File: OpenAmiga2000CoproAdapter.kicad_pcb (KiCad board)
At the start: 2 copper layers, 188.6 x 110.4 mm, 75 parts, among them CN1 A2000_COPRO_SLOT, P1 CONN_2, P10 CONN_1, P11 CONN_1, P12 CONN_1, P13 CONN_1, P14 CONN_1, P15 CONN_1, P2 CONN_2, P3 CONN_2, P4 CONN_2, P5 CONN_1, P6 CONN_1, P7 CONN_1, P8 CONN_1, P9 CONN_1, P99 OSHW_LOGO, U1 68000D, U10 Spare, U11 74HCT00, U12 74HCT27, U13 74HCT74, U14 74F86, U15 74F74, U16 74HCT04, U17 74HCT112, U18 74F157, U19 74F157, U2 AS6C4008-55PCN, U3 AS6C4008-55PCN, U4 AS6C4008-55PCN, U5 AS6C4008-55PCN, U6 74HCT00, U7 74HCT32, U8 74HCT32, U9 74LS05

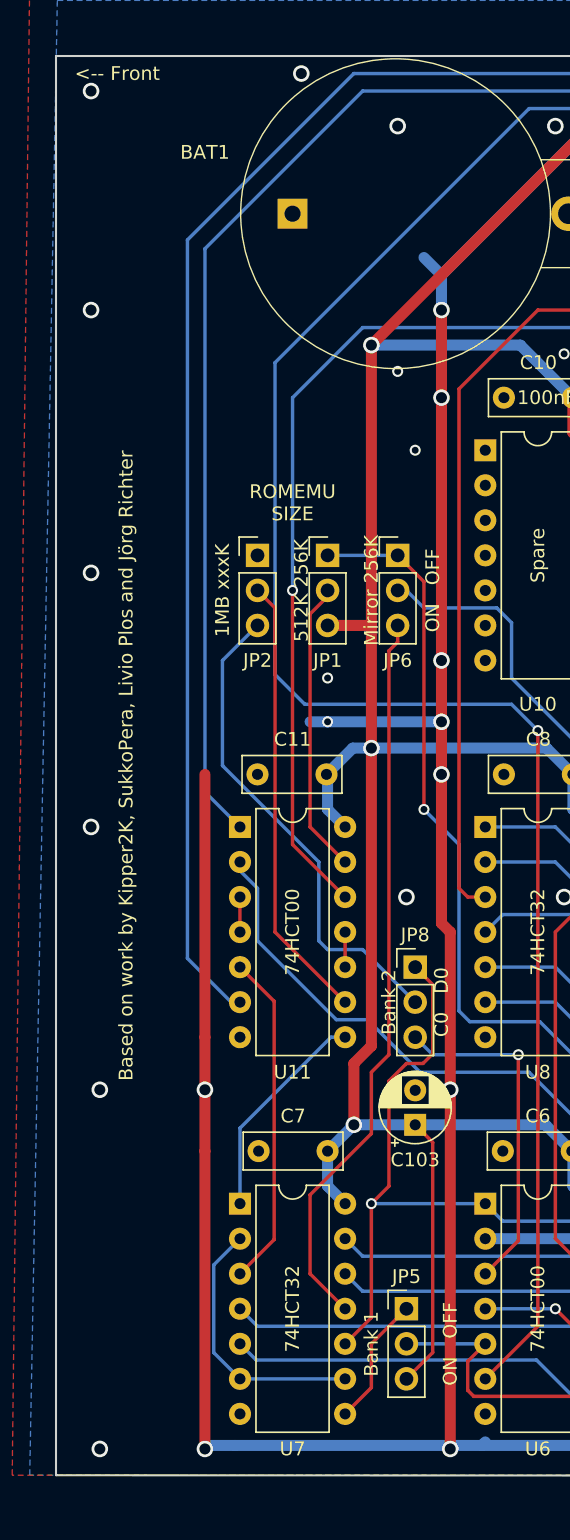
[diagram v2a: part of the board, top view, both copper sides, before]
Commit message: more via fixing
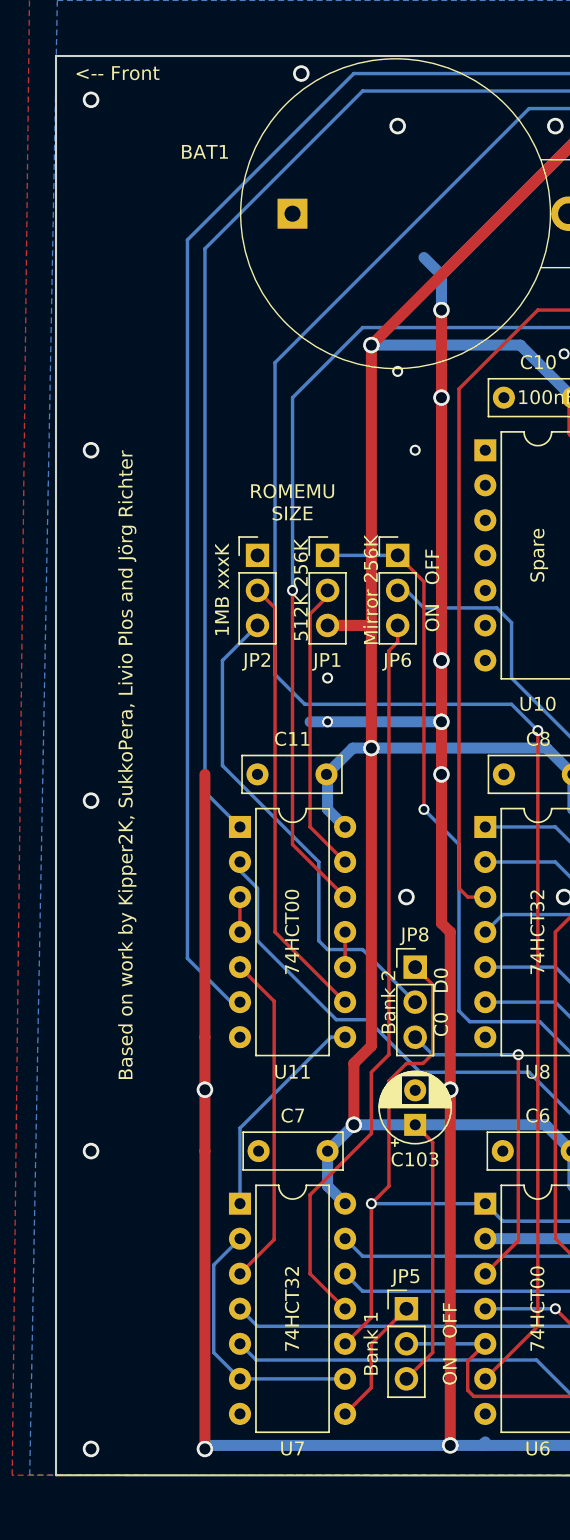
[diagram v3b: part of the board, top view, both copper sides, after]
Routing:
- net GND: track 1168.9 -> 1168.5 mm, vias 158 -> 157
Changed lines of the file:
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@@
   (segment (start 108.458 138.1125) (end 107.2515 136.906) (width 0.8) (layer B.Cu) (net 1))
   (segment (start 93.0275 136.906) (end 90.106496 136.906) (width 0.8) (layer B.Cu) (net 1))
-  (segment (start 90.106504 136.905992) (end 90.106496 136.906) (width 0.8) (layer B.Cu) (net 1))
-  (segment (start 90.106504 136.906) (end 90.106504 136.905992) (width 0.8) (layer B.Cu) (net 1))
   (segment (start 72.3265 136.652) (end 72.0725 136.906) (width 0.8) (layer B.Cu) (net 1))
-  (segment (start 72.0725 136.906) (end 90.106504 136.906) (width 0.8) (layer B.Cu) (net 1))
-  (segment (start 72.0725 136.906) (end 69.4055 136.906) (width 0.8) (layer B.Cu) (net 1))
   (segment (start 52.0065 107.315) (end 52.0065 115.57) (width 0.8) (layer F.Cu) (net 1))
   (segment (start 52.0065 115.57) (end 52.0065 136.906) (width 0.8) (layer F.Cu) (net 1))
-  (segment (start 54.1655 136.906) (end 52.0065 136.906) (width 0.8) (layer B.Cu) (net 1))
   (via (at 52.0065 137.16) (size 1.2) (drill 0.8) (layers F.Cu B.Cu) (net 1))
-  (via (at 69.7865 137.16) (size 1.2) (drill 0.8) (layers F.Cu B.Cu) (net 1))
-  (segment (start 54.1655 136.906) (end 69.7865 136.906) (width 0.8) (layer B.Cu) (net 1))
-  (segment (start 69.7865 136.906) (end 69.786502 136.906002) (width 0.8) (layer B.Cu) (net 1))
   (segment (start 52.0065 107.315) (end 52.0065 88.265) (width 0.8) (layer F.Cu) (net 1))
   (via (at 66.6115 97.155) (size 1.2) (drill 0.8) (layers F.Cu B.Cu) (net 1))
@@
   (via (at 69.7865 111.125) (size 1.2) (drill 0.8) (layers F.Cu B.Cu) (net 1))
   (segment (start 187.2615 103.505) (end 187.2615 103.505) (width 0.8) (layer F.Cu) (net 1))
-  (via (at 187.2615 103.505) (size 1.2) (drill 0.8) (layers F.Cu B.Cu) (net 1) (status 1000000))
+  (via (at 187.2615 103.505) (size 1.2) (drill 0.8) (layers F.Cu B.Cu) (net 1))
   (segment (start 189.8015 86.995) (end 189.8015 84.455) (width 0.8) (layer B.Cu) (net 1))
   (segment (start 187.2615 84.455) (end 189.8015 84.455) (width 0.8) (layer B.Cu) (net 1))
@@
   (segment (start 213.9315 45.72) (end 213.9315 45.72) (width 0.8) (layer B.Cu) (net 1))
   (via (at 213.9315 45.72) (size 1.2) (drill 0.8) (layers F.Cu B.Cu) (net 1))
-  (via (at 44.3865 137.16) (size 1.2) (drill 0.8) (layers F.Cu B.Cu) (net 1))
-  (via (at 44.3865 111.125) (size 1.2) (drill 0.8) (layers F.Cu B.Cu) (net 1))
-  (via (at 43.7515 92.075) (size 1.2) (drill 0.8) (layers F.Cu B.Cu) (net 1))
+  (via (at 43.7515 137.16) (size 1.2) (drill 0.8) (layers F.Cu B.Cu) (net 1))
+  (via (at 43.7515 115.57) (size 1.2) (drill 0.8) (layers F.Cu B.Cu) (net 1))
+  (via (at 43.7515 90.17) (size 1.2) (drill 0.8) (layers F.Cu B.Cu) (net 1))
   (via (at 208.8515 52.705) (size 1.2) (drill 0.8) (layers F.Cu B.Cu) (net 1))
   (via (at 205.0415 57.785) (size 1.2) (drill 0.8) (layers F.Cu B.Cu) (net 1))
@@
   (via (at 118.6815 109.22) (size 1.2) (drill 0.8) (layers F.Cu B.Cu) (net 1))
   (via (at 52.0065 111.125) (size 1.2) (drill 0.8) (layers F.Cu B.Cu) (net 1))
-  (via (at 43.7515 54.61) (size 1.2) (drill 0.8) (layers F.Cu B.Cu) (net 1))
+  (via (at 43.7515 64.77) (size 1.2) (drill 0.8) (layers F.Cu B.Cu) (net 1))
   (via (at 169.4815 137.795) (size 0.8) (drill 0.5) (layers F.Cu B.Cu) (net 1))
   (segment (start 168.8465 137.16) (end 168.724159 137.037659) (width 0.8) (layer F.Cu) (net 1))
@@
   (via (at 83.7565 57.15) (size 1.2) (drill 0.8) (layers F.Cu B.Cu) (net 1))
   (via (at 184.7215 64.77) (size 1.2) (drill 0.8) (layers F.Cu B.Cu) (net 1))
-  (via (at 43.7515 38.735) (size 1.2) (drill 0.8) (layers F.Cu B.Cu) (net 1))
+  (via (at 43.7515 39.37) (size 1.2) (drill 0.8) (layers F.Cu B.Cu) (net 1))
   (via (at 58.9915 37.465) (size 1.2) (drill 0.8) (layers F.Cu B.Cu) (net 1))
   (via (at 194.8815 48.26) (size 1.2) (drill 0.8) (layers F.Cu B.Cu) (net 1))
@@
   (segment (start 187.2615 122.555) (end 187.2615 127.635) (width 0.8) (layer B.Cu) (net 1))
   (via (at 187.2615 127.635) (size 1.2) (drill 0.8) (layers F.Cu B.Cu) (net 1))
-  (via (at 43.7515 73.66) (size 1.2) (drill 0.8) (layers F.Cu B.Cu) (net 1))
   (via (at 174.5615 82.55) (size 1.2) (drill 0.8) (layers F.Cu B.Cu) (net 1))
   (via (at 184.0865 43.815) (size 1.2) (drill 0.8) (layers F.Cu B.Cu) (net 1))
   (via (at 179.6415 113.665) (size 1.2) (drill 0.8) (layers F.Cu B.Cu) (net 1))
+  (segment (start 90.106504 136.905992) (end 90.106496 136.906) (width 0.8) (layer B.Cu) (net 1))
+  (segment (start 90.106504 136.906) (end 90.106504 136.905992) (width 0.8) (layer B.Cu) (net 1))
+  (segment (start 72.0725 136.906) (end 90.106504 136.906) (width 0.8) (layer B.Cu) (net 1))
+  (via (at 69.786502 136.905998) (size 1.2) (drill 0.8) (layers F.Cu B.Cu) (net 1))
+  (segment (start 72.0725 136.906) (end 69.786504 136.906) (width 0.8) (layer B.Cu) (net 1))
+  (segment (start 69.786504 136.906) (end 69.786502 136.905998) (width 0.8) (layer B.Cu) (net 1))
+  (segment (start 69.786498 136.905998) (end 69.786502 136.906002) (width 0.8) (layer B.Cu) (net 1))
+  (segment (start 52.006502 136.905998) (end 69.786498 136.905998) (width 0.8) (layer B.Cu) (net 1))
+  (segment (start 52.0065 136.906) (end 52.006502 136.905998) (width 0.8) (layer B.Cu) (net 1))
   (segment (start 126.238 108.6485) (end 126.3015 108.585) (width 0.8) (layer F.Cu) (net 2))
   (segment (start 126.238 112.0775) (end 126.238 108.6485) (width 0.8) (layer F.Cu) (net 2))

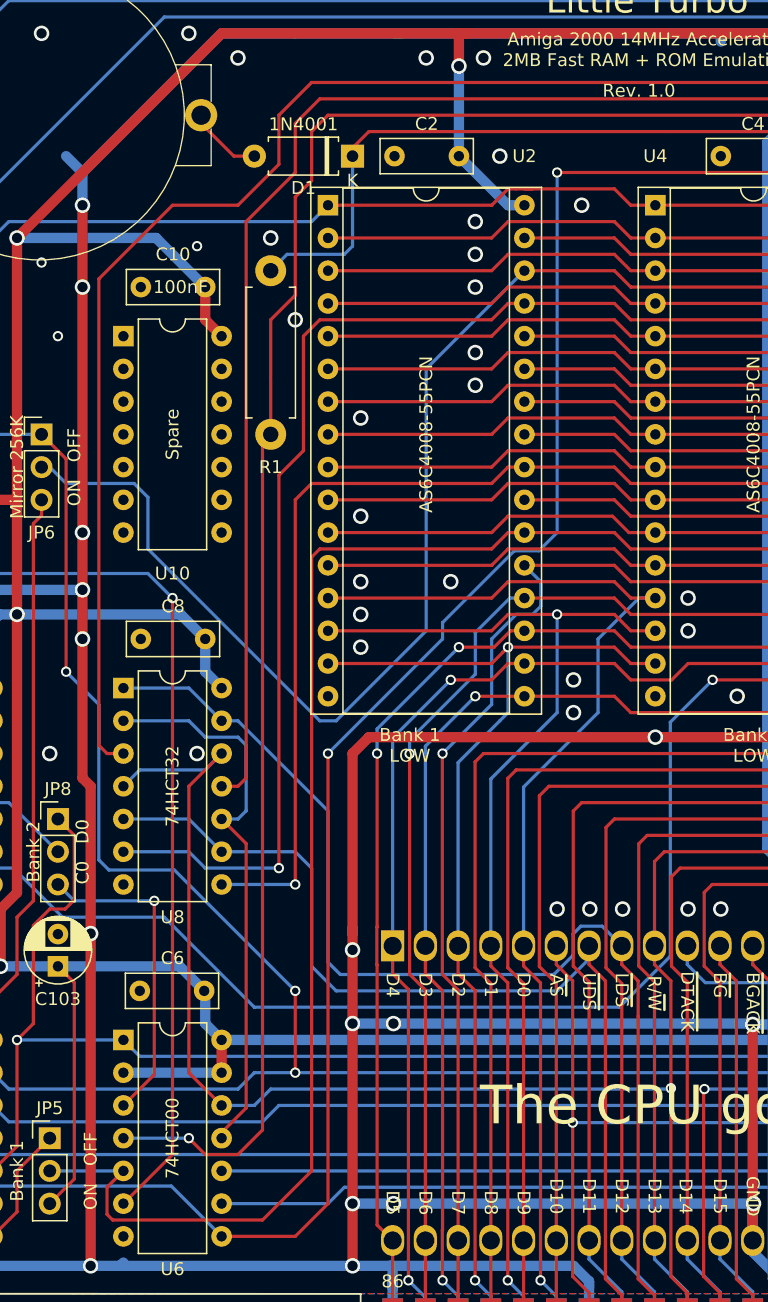
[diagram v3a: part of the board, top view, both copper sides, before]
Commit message: fix silkscreen label
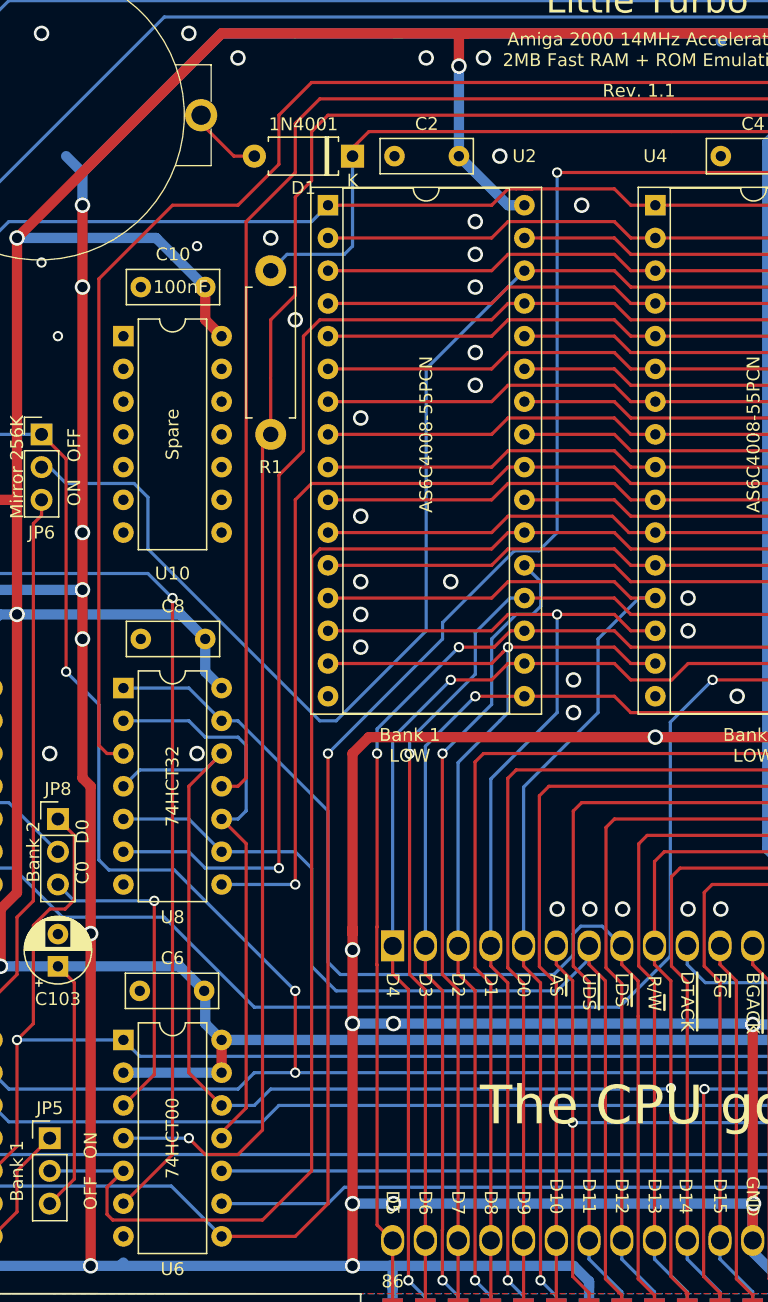
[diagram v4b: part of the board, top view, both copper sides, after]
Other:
- board text added: "OFF ON"
- board text added: "Rev. 1.1"
- board text removed: "Rev. 1.0"

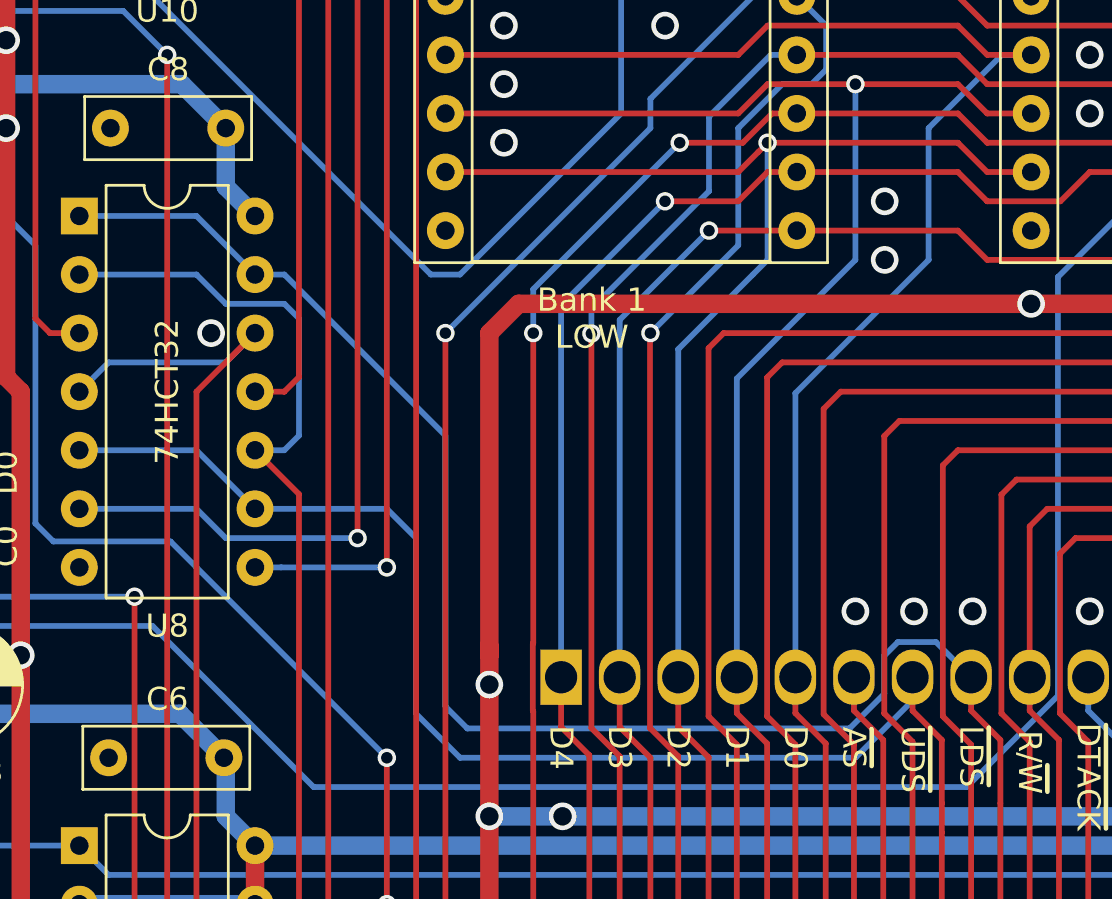
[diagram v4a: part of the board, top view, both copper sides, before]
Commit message: fix uds lds mixup
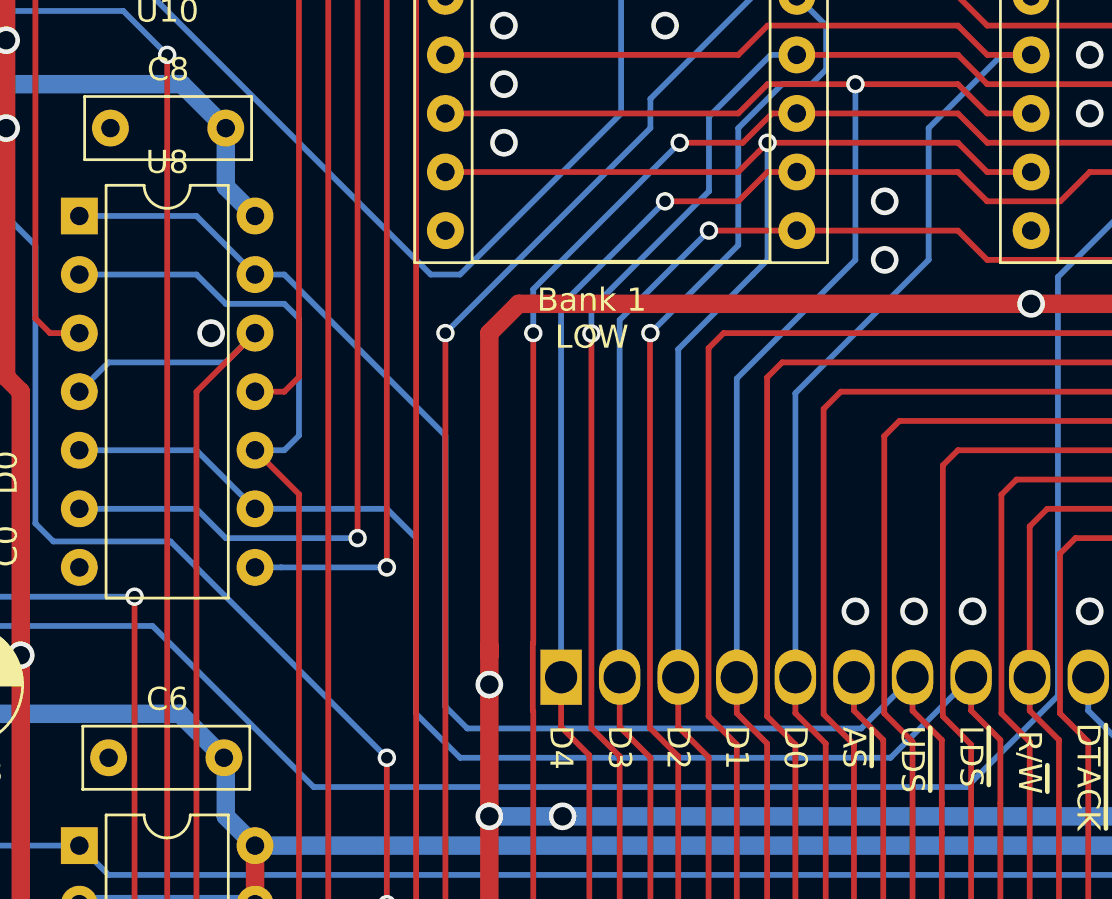
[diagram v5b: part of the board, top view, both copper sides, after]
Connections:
- U2 pad 24: /Memory/~UOE -> /Memory/~LOE
- U2 pad 29: /Memory/~UWE -> /Memory/~LWE
- U3 pad 24: /Memory/~LOE -> /Memory/~UOE
- U3 pad 29: /Memory/~LWE -> /Memory/~UWE
- U4 pad 24: /Memory/~UOE -> /Memory/~LOE
- U4 pad 29: /Memory/~UWE -> /Memory/~LWE
- U5 pad 24: /Memory/~LOE -> /Memory/~UOE
- U5 pad 29: /Memory/~LWE -> /Memory/~UWE
- U8 pad 1: /~lds -> /~uds
- U8 pad 11: /Memory/~LWE -> /Memory/~UWE
- U8 pad 13: /~lds -> /~uds
- U8 pad 3: /Memory/~LOE -> /Memory/~UOE
- U8 pad 5: /~uds -> /~lds
- U8 pad 6: /Memory/~UWE -> /Memory/~LWE
- U8 pad 8: /Memory/~UOE -> /Memory/~LOE
- U8 pad 9: /~uds -> /~lds
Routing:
- net /Memory/~UOE: track 81.5 -> 214.2 mm, vias 1 -> 0
- net /Memory/~LOE: track 214.2 -> 81.5 mm, vias 0 -> 1
- net /Memory/~UWE: track 99.9 -> 192.0 mm, vias 1 -> 0
- net /Memory/~LWE: track 192.0 -> 99.9 mm, vias 0 -> 1
- net /~lds: track 90.6 -> 82.8 mm
- net /~uds: track 79.8 -> 85.8 mm
